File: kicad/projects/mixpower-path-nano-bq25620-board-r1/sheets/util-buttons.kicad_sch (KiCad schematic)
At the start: 17 parts, among them SW1 TS-A002, SW2 TS-A002, SW3 TS-A002, U11 RT9829GQW, U12 RT9829GQW

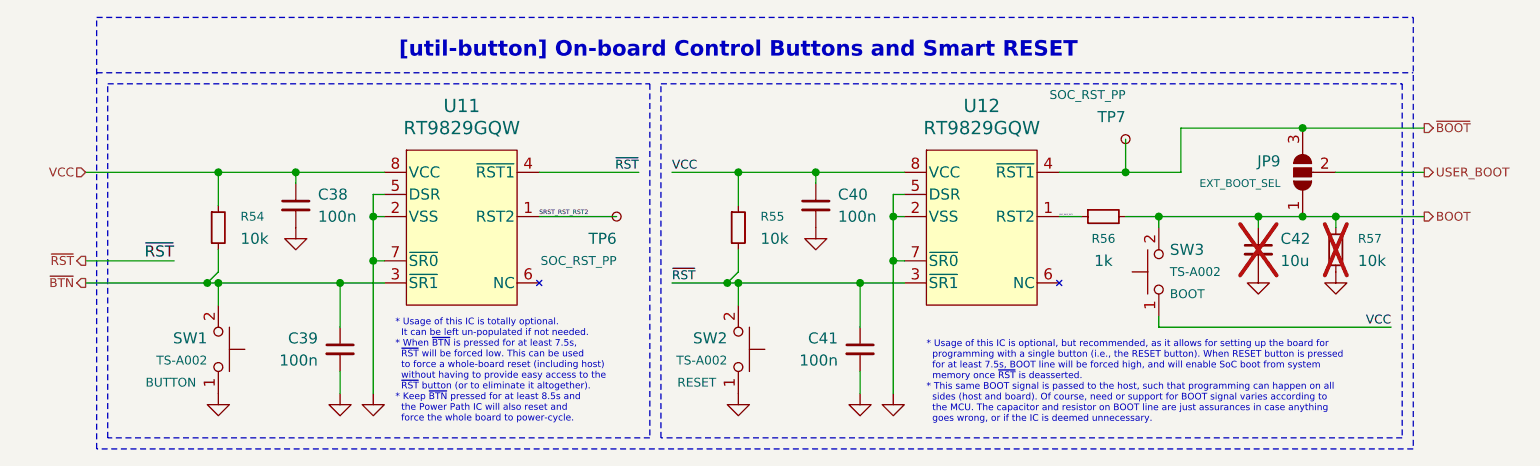
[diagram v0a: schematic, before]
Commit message: feat: rework schematics and add proper calculations
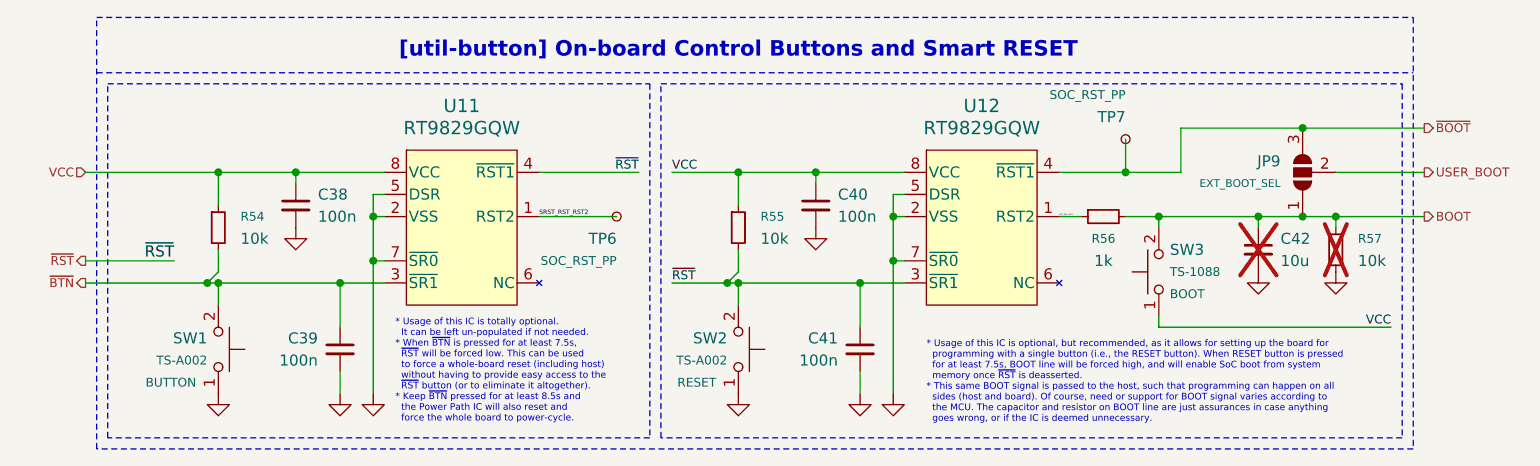
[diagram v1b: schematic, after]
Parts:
- SW3: value TS-A002 -> TS-1088
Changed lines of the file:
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@@
 		)
 		(instances
-			(project "mixpower-path-mini-bq25620-board-r1"
+			(project "mixpower-path-nano-bq25620-board-r1"
 				(path "/2e43857b-9bf9-460c-948c-ec2cf8a8d6b4/ff152d90-3a9a-4696-84f9-0fc6d9a5b4f4"
 					(reference "C42")
@@
 		)
 		(instances
-			(project "mixpower-path-mini-bq25620-board-r1"
+			(project "mixpower-path-nano-bq25620-board-r1"
 				(path "/2e43857b-9bf9-460c-948c-ec2cf8a8d6b4/ff152d90-3a9a-4696-84f9-0fc6d9a5b4f4"
 					(reference "JP9")
@@
 		)
 		(instances
-			(project "mixpower-path-mini-bq25620-board-r1"
+			(project "mixpower-path-nano-bq25620-board-r1"
 				(path "/2e43857b-9bf9-460c-948c-ec2cf8a8d6b4/ff152d90-3a9a-4696-84f9-0fc6d9a5b4f4"
 					(reference "C40")
@@
 		)
 		(instances
-			(project "mixpower-path-mini-bq25620-board-r1"
+			(project "mixpower-path-nano-bq25620-board-r1"
 				(path "/2e43857b-9bf9-460c-948c-ec2cf8a8d6b4/ff152d90-3a9a-4696-84f9-0fc6d9a5b4f4"
 					(reference "#PWR071")
@@
 		)
 		(instances
-			(project "mixpower-path-mini-bq25620-board-r1"
+			(project "mixpower-path-nano-bq25620-board-r1"
 				(path "/2e43857b-9bf9-460c-948c-ec2cf8a8d6b4/ff152d90-3a9a-4696-84f9-0fc6d9a5b4f4"
 					(reference "#PWR065")
@@
 		)
 		(instances
-			(project "mixpower-path-mini-bq25620-board-r1"
+			(project "mixpower-path-nano-bq25620-board-r1"
 				(path "/2e43857b-9bf9-460c-948c-ec2cf8a8d6b4/ff152d90-3a9a-4696-84f9-0fc6d9a5b4f4"
 					(reference "TP6")
@@
 		)
 		(instances
-			(project "mixpower-path-mini-bq25620-board-r1"
+			(project "mixpower-path-nano-bq25620-board-r1"
 				(path "/2e43857b-9bf9-460c-948c-ec2cf8a8d6b4/ff152d90-3a9a-4696-84f9-0fc6d9a5b4f4"
 					(reference "C41")
@@
 		)
 		(instances
-			(project "mixpower-path-mini-bq25620-board-r1"
+			(project "mixpower-path-nano-bq25620-board-r1"
 				(path "/2e43857b-9bf9-460c-948c-ec2cf8a8d6b4/ff152d90-3a9a-4696-84f9-0fc6d9a5b4f4"
 					(reference "R54")
@@
 		)
 		(instances
-			(project "mixpower-path-mini-bq25620-board-r1"
+			(project "mixpower-path-nano-bq25620-board-r1"
 				(path "/2e43857b-9bf9-460c-948c-ec2cf8a8d6b4/ff152d90-3a9a-4696-84f9-0fc6d9a5b4f4"
 					(reference "U12")
@@
 		)
 		(instances
-			(project "mixpower-path-mini-bq25620-board-r1"
+			(project "mixpower-path-nano-bq25620-board-r1"
 				(path "/2e43857b-9bf9-460c-948c-ec2cf8a8d6b4/ff152d90-3a9a-4696-84f9-0fc6d9a5b4f4"
 					(reference "U11")
@@
 		)
 		(instances
-			(project "mixpower-path-mini-bq25620-board-r1"
+			(project "mixpower-path-nano-bq25620-board-r1"
 				(path "/2e43857b-9bf9-460c-948c-ec2cf8a8d6b4/ff152d90-3a9a-4696-84f9-0fc6d9a5b4f4"
 					(reference "R57")
@@
 		)
 		(instances
-			(project "mixpower-path-mini-bq25620-board-r1"
+			(project "mixpower-path-nano-bq25620-board-r1"
 				(path "/2e43857b-9bf9-460c-948c-ec2cf8a8d6b4/ff152d90-3a9a-4696-84f9-0fc6d9a5b4f4"
 					(reference "SW2")
@@
 		)
 		(instances
-			(project "mixpower-path-mini-bq25620-board-r1"
+			(project "mixpower-path-nano-bq25620-board-r1"
 				(path "/2e43857b-9bf9-460c-948c-ec2cf8a8d6b4/ff152d90-3a9a-4696-84f9-0fc6d9a5b4f4"
 					(reference "#PWR069")
@@
 		)
 		(instances
-			(project "mixpower-path-mini-bq25620-board-r1"
+			(project "mixpower-path-nano-bq25620-board-r1"
 				(path "/2e43857b-9bf9-460c-948c-ec2cf8a8d6b4/ff152d90-3a9a-4696-84f9-0fc6d9a5b4f4"
 					(reference "#PWR070")
@@
 		)
 		(instances
-			(project "mixpower-path-mini-bq25620-board-r1"
+			(project "mixpower-path-nano-bq25620-board-r1"
 				(path "/2e43857b-9bf9-460c-948c-ec2cf8a8d6b4/ff152d90-3a9a-4696-84f9-0fc6d9a5b4f4"
 					(reference "#PWR073")
@@
 		)
 		(instances
-			(project "mixpower-path-mini-bq25620-board-r1"
+			(project "mixpower-path-nano-bq25620-board-r1"
 				(path "/2e43857b-9bf9-460c-948c-ec2cf8a8d6b4/ff152d90-3a9a-4696-84f9-0fc6d9a5b4f4"
 					(reference "#PWR072")
@@
 			)
 		)
-		(property "Value" "TS-A002"
+		(property "Value" "TS-1088"
 			(at 182.88 80.0099 90)
 			(show_name no)
@@
 		)
 		(instances
-			(project "mixpower-path-mini-bq25620-board-r1"
+			(project "mixpower-path-nano-bq25620-board-r1"
 				(path "/2e43857b-9bf9-460c-948c-ec2cf8a8d6b4/ff152d90-3a9a-4696-84f9-0fc6d9a5b4f4"
 					(reference "SW3")
@@
 		)
 		(instances
-			(project "mixpower-path-mini-bq25620-board-r1"
+			(project "mixpower-path-nano-bq25620-board-r1"
 				(path "/2e43857b-9bf9-460c-948c-ec2cf8a8d6b4/ff152d90-3a9a-4696-84f9-0fc6d9a5b4f4"
 					(reference "C39")
@@
 		)
 		(instances
-			(project "mixpower-path-mini-bq25620-board-r1"
+			(project "mixpower-path-nano-bq25620-board-r1"
 				(path "/2e43857b-9bf9-460c-948c-ec2cf8a8d6b4/ff152d90-3a9a-4696-84f9-0fc6d9a5b4f4"
 					(reference "#PWR074")
@@
 		)
 		(instances
-			(project "mixpower-path-mini-bq25620-board-r1"
+			(project "mixpower-path-nano-bq25620-board-r1"
 				(path "/2e43857b-9bf9-460c-948c-ec2cf8a8d6b4/ff152d90-3a9a-4696-84f9-0fc6d9a5b4f4"
 					(reference "SW1")
@@
 		)
 		(instances
-			(project "mixpower-path-mini-bq25620-board-r1"
+			(project "mixpower-path-nano-bq25620-board-r1"
 				(path "/2e43857b-9bf9-460c-948c-ec2cf8a8d6b4/ff152d90-3a9a-4696-84f9-0fc6d9a5b4f4"
 					(reference "#PWR066")
@@
 		)
 		(instances
-			(project "mixpower-path-mini-bq25620-board-r1"
+			(project "mixpower-path-nano-bq25620-board-r1"
 				(path "/2e43857b-9bf9-460c-948c-ec2cf8a8d6b4/ff152d90-3a9a-4696-84f9-0fc6d9a5b4f4"
 					(reference "TP7")
@@
 		)
 		(instances
-			(project "mixpower-path-mini-bq25620-board-r1"
+			(project "mixpower-path-nano-bq25620-board-r1"
 				(path "/2e43857b-9bf9-460c-948c-ec2cf8a8d6b4/ff152d90-3a9a-4696-84f9-0fc6d9a5b4f4"
 					(reference "#PWR067")
@@
 		)
 		(instances
-			(project "mixpower-path-mini-bq25620-board-r1"
+			(project "mixpower-path-nano-bq25620-board-r1"
 				(path "/2e43857b-9bf9-460c-948c-ec2cf8a8d6b4/ff152d90-3a9a-4696-84f9-0fc6d9a5b4f4"
 					(reference "C38")
@@
 		)
 		(instances
-			(project "mixpower-path-mini-bq25620-board-r1"
+			(project "mixpower-path-nano-bq25620-board-r1"
 				(path "/2e43857b-9bf9-460c-948c-ec2cf8a8d6b4/ff152d90-3a9a-4696-84f9-0fc6d9a5b4f4"
 					(reference "#PWR068")
@@
 		)
 		(instances
-			(project "mixpower-path-mini-bq25620-board-r1"
+			(project "mixpower-path-nano-bq25620-board-r1"
 				(path "/2e43857b-9bf9-460c-948c-ec2cf8a8d6b4/ff152d90-3a9a-4696-84f9-0fc6d9a5b4f4"
 					(reference "R56")
@@
 		)
 		(instances
-			(project "mixpower-path-mini-bq25620-board-r1"
+			(project "mixpower-path-nano-bq25620-board-r1"
 				(path "/2e43857b-9bf9-460c-948c-ec2cf8a8d6b4/ff152d90-3a9a-4696-84f9-0fc6d9a5b4f4"
 					(reference "R55")
